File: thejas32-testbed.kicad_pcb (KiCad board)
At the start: 4 copper layers, 81.4 x 89.2 mm, 100 parts, among them J1 Conn_01x04, J10 Conn_02x10_Odd_Even, J11 Conn_01x03, J12 Conn_02x20_Odd_Even, J13 Conn_01x03, J2 USB_B_Micro, J3 Conn_02x03_Odd_Even, J4 Conn_02x05_Odd_Even, J6 Conn_01x10, J7 Conn_01x05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

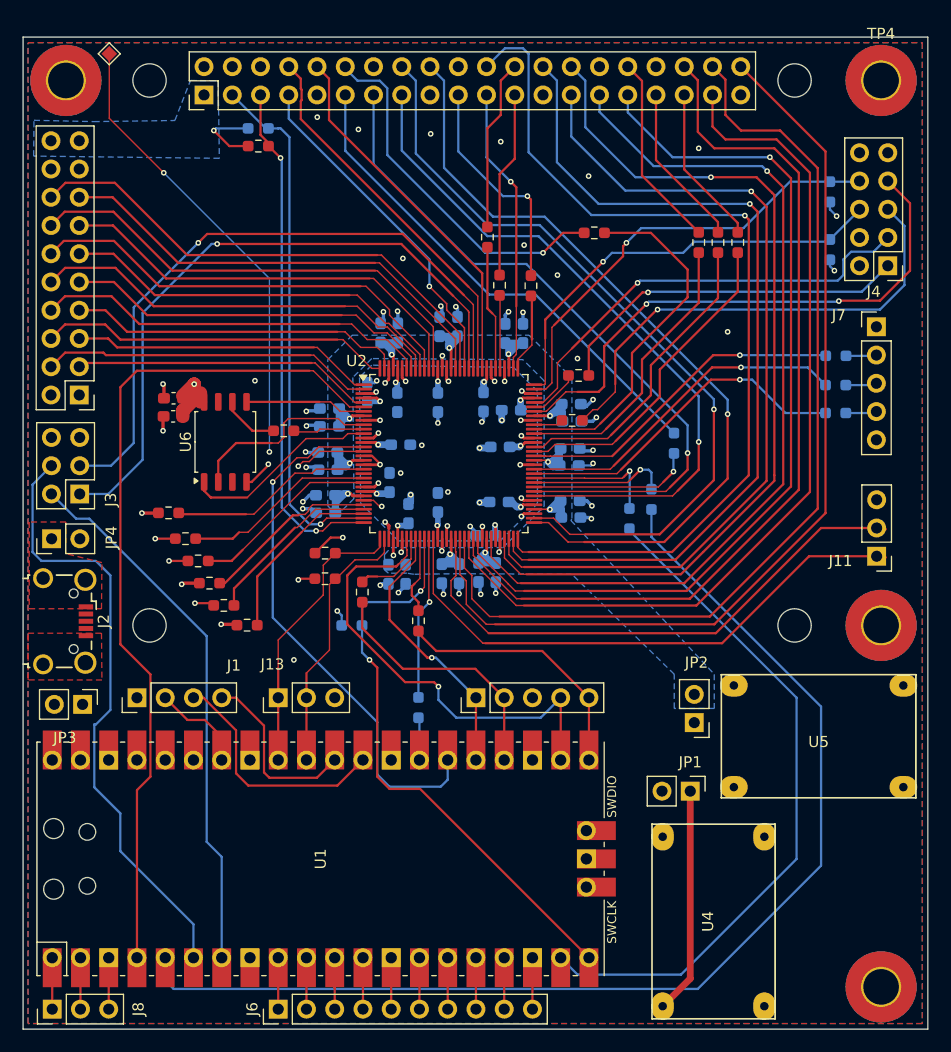
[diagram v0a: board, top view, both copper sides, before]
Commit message: Heartbeat moved near mini360s
Also corrected the file path of the 3D model for the
flash IC
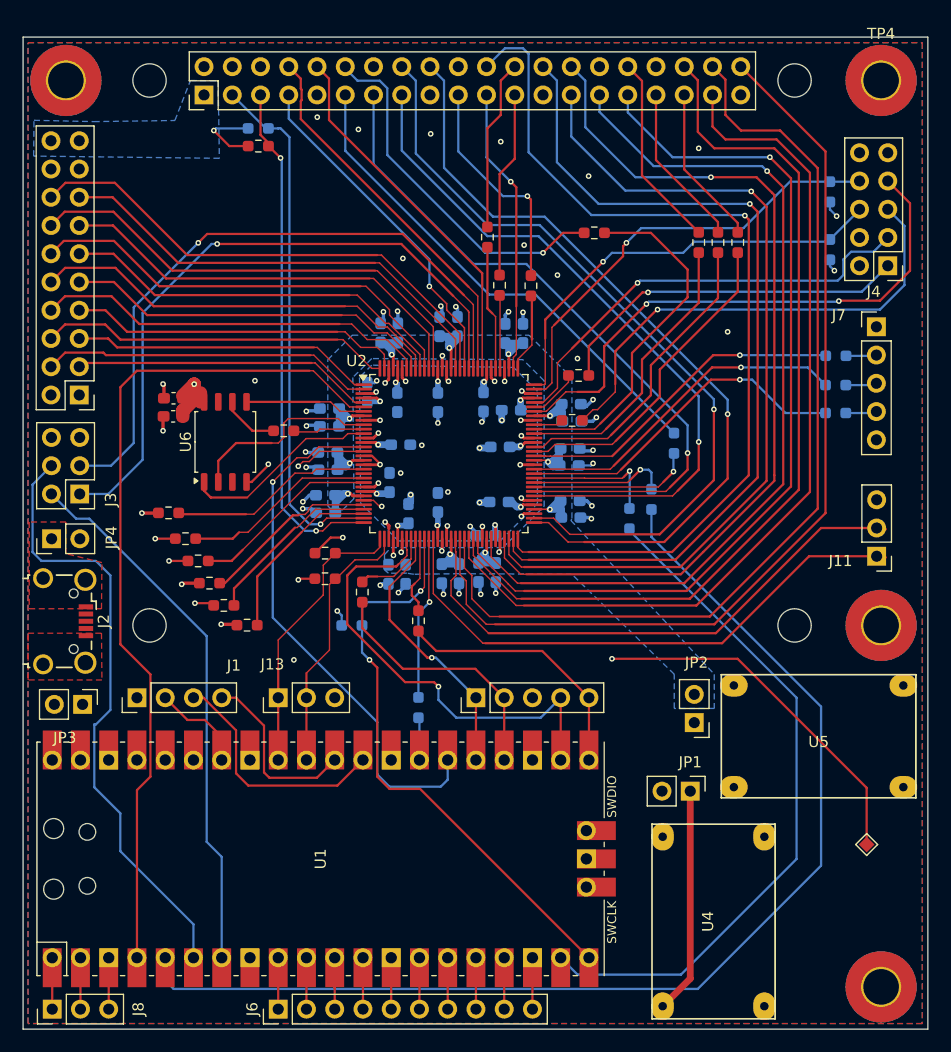
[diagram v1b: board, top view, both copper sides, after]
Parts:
- moved TP7 98.5 mm to (193.1, 139.2)
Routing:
- net Net-(U2-PROC_HEART_BEAT): track 51.3 -> 83.0 mm, vias 3 -> 2
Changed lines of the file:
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@@
 	(footprint "TestPoint:TestPoint_Pad_1.0x1.0mm"
 		(layer "F.Cu")
-		(at 125 68.1 45)
+		(at 193.1 139.2 45)
 		(descr "SMD rectangular pad as test Point, square 1.0mm side length")
 		(tags "test point SMD pad rectangle square")
@@
 		)
 		(property "Footprint" "Package_SO:SOIC-8_5.23x5.23mm_P1.27mm"
-			(at 0 0 90)
+			(at 0.5 -11 90)
 			(unlocked yes)
 			(layer "F.Fab")
@@
 		)
 		(property "Datasheet" "http://www.winbond.com/resource-files/w25q32jv%20revg%2003272018%20plus.pdf"
-			(at 0 0 90)
+			(at 0.5 -6.5 90)
 			(unlocked yes)
 			(layer "F.Fab")
@@
 		)
 		(property "Description" "16Mb Serial Flash Memory, Standard/Dual/Quad SPI, SOIC-8"
-			(at 0 0 90)
+			(at 0.5 -15 90)
 			(unlocked yes)
 			(layer "F.Fab")
@@
 			(pintype "power_in")
 		)
-		(model "${KICAD7_3DMODEL_DIR}/Package_SO.3dshapes/SOIC-8_5.23x5.23mm_P1.27mm.wrl"
+		(model "${KICAD_3DMODEL_DIR}/Package_SO.3dshapes/SOIC-8_5.275x5.275mm_P1.27mm.wrl"
 			(offset
 				(xyz 0 0 0)
@@
 	)
 	(segment
-		(start 125 73.9)
-		(end 125 68.1)
-		(width 0.127)
+		(start 193.1 134.1)
+		(end 193.1 139.2)
+		(width 0.2032)
+		(layer "F.Cu")
+		(net 124)
+	)
+	(segment
+		(start 181.5 122.5)
+		(end 193.1 134.1)
+		(width 0.2032)
 		(layer "F.Cu")
 		(net 124)
@@
 	)
 	(segment
-		(start 142.986756 104.7666)
-		(end 143.900856 103.8525)
-		(width 0.127)
+		(start 170.2 122.5)
+		(end 181.5 122.5)
+		(width 0.2032)
 		(layer "F.Cu")
 		(net 124)
 	)
 	(segment
-		(start 129.9 78.8)
-		(end 125 73.9)
+		(start 142.986756 104.7666)
+		(end 143.900856 103.8525)
 		(width 0.127)
 		(layer "F.Cu")
@@
 	)
 	(via
-		(at 129.9 78.8)
+		(at 141.996208 105.184898)
 		(size 0.508)
 		(drill 0.254)
@@
 	)
 	(via
-		(at 141.996208 105.184898)
+		(at 170.2 122.5)
 		(size 0.508)
 		(drill 0.254)
@@
 		(net 124)
 	)
-	(via
-		(at 139.4 103.9)
-		(size 0.508)
-		(drill 0.254)
-		(layers "F.Cu" "B.Cu")
+	(segment
+		(start 141.8412 117.6412)
+		(end 153.250937 117.6412)
+		(width 0.2032)
+		(layer "In2.Cu")
 		(net 124)
 	)
 	(segment
-		(start 139.4 103.9)
-		(end 140.684898 105.184898)
-		(width 0.127)
+		(start 170.1 122.5)
+		(end 170.2 122.5)
+		(width 0.2032)
 		(layer "In2.Cu")
 		(net 124)
 	)
 	(segment
-		(start 140.684898 105.184898)
-		(end 141.996208 105.184898)
-		(width 0.127)
+		(start 140.9 106.2)
+		(end 140.9 116.7)
+		(width 0.2032)
 		(layer "In2.Cu")
 		(net 124)
 	)
 	(segment
-		(start 139.4 103.9)
-		(end 139.4 88.3)
-		(width 0.127)
-		(layer "B.Cu")
+		(start 165.5588 117.9588)
+		(end 170.1 122.5)
+		(width 0.2032)
+		(layer "In2.Cu")
 		(net 124)
 	)
 	(segment
-		(start 139.4 88.3)
-		(end 129.9 78.8)
-		(width 0.127)
-		(layer "B.Cu")
+		(start 153.568537 117.9588)
+		(end 165.5588 117.9588)
+		(width 0.2032)
+		(layer "In2.Cu")
+		(net 124)
+	)
+	(segment
+		(start 141.996208 105.184898)
+		(end 141.915102 105.184898)
+		(width 0.2032)
+		(layer "In2.Cu")
+		(net 124)
+	)
+	(segment
+		(start 140.9 116.7)
+		(end 141.8412 117.6412)
+		(width 0.2032)
+		(layer "In2.Cu")
+		(net 124)
+	)
+	(segment
+		(start 141.915102 105.184898)
+		(end 140.9 106.2)
+		(width 0.2032)
+		(layer "In2.Cu")
+		(net 124)
+	)
+	(segment
+		(start 153.250937 117.6412)
+		(end 153.568537 117.9588)
+		(width 0.2032)
+		(layer "In2.Cu")
 		(net 124)
 	)
@@
 			(pts
 				(xy 163.3 98.766666) (xy 163.3 108.8) (xy 160.368182 111.8) (xy 150.75 111.8) (xy 145.2 114.8875)
-				(xy 142.6 117.4) (xy 140.4 116.9) (xy 141.5 115) (xy 143.6125 113) (xy 145.7 111.2) (xy 147.45 107.75)
+				(xy 143.5 116.5) (xy 141.4 116.5) (xy 141.4 114.9) (xy 143.6125 113) (xy 145.7 111.2) (xy 147.45 107.75)
 				(xy 147.45 97.924418) (xy 149.3 96.45) (xy 161.295195 96.45)
 			)

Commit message: Cleanup and beautification for review.
Added silkscreen for all components.
Grouped schematic for reading clarity.
No circuit level changes, few nets renamed.
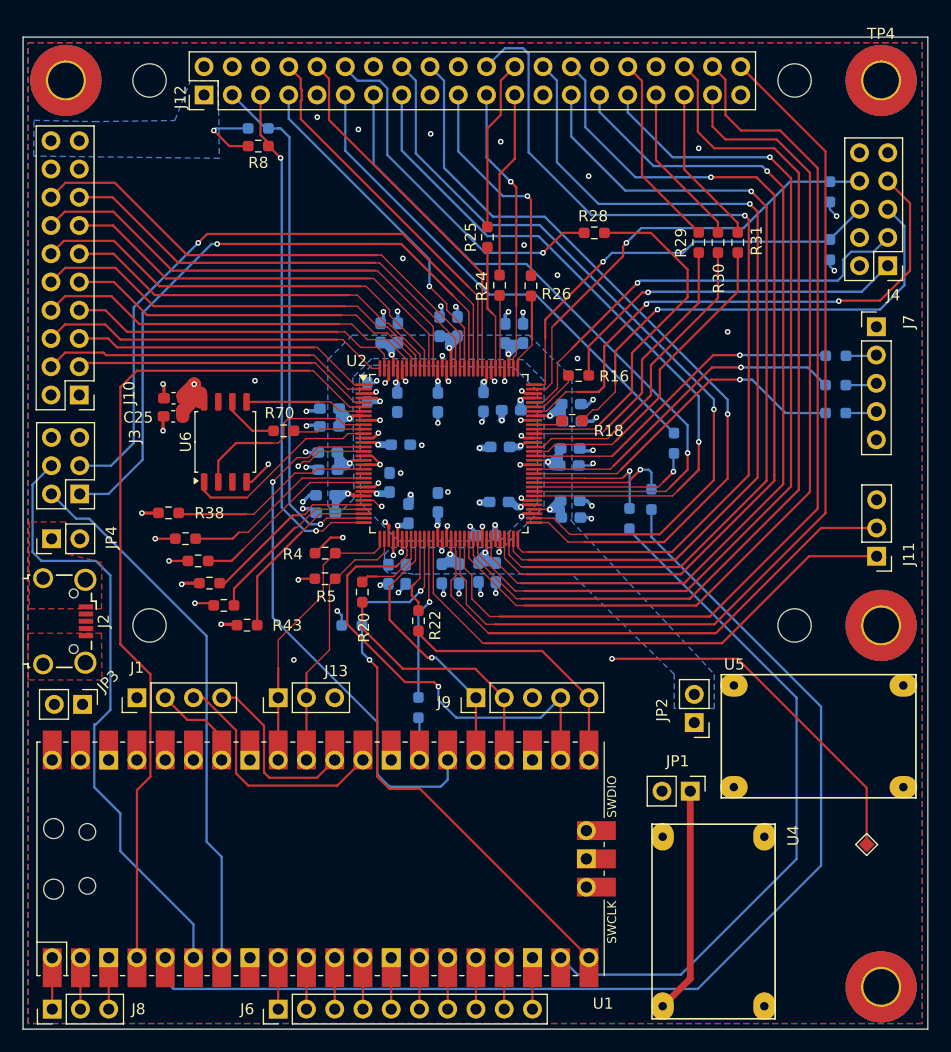
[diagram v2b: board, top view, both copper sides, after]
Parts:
- R1, R70: value 27E -> 10E
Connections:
- net Net-(J11-Pin_1) renamed MCU_UART1_TX
- net Net-(J11-Pin_2) renamed MCU_UART1_RX
- J3 pad 1: Net-(J3-Pin_1) -> MCU_BOOT_UART_TX
- J3 pad 2: MCU_BOOT_UART_TX -> MCU_BOOT_UART_TX_PICO
- J3 pad 3: Net-(J3-Pin_3) -> MCU_BOOT_UART_RX
- J3 pad 4: MCU_BOOT_UART_RX -> MCU_BOOT_UART_RX_PICO
- U1 pad 6: MCU_BOOT_UART_RX -> MCU_BOOT_UART_RX_PICO
- U1 pad 7: MCU_BOOT_UART_TX -> MCU_BOOT_UART_TX_PICO
- U2 pad 107: Net-(J3-Pin_3) -> MCU_BOOT_UART_RX
- U2 pad 108: Net-(J3-Pin_1) -> MCU_BOOT_UART_TX
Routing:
- net Net-(J3-Pin_1): track 59.7 -> 0.00 mm, vias 1 -> 0
- net Net-(J3-Pin_3): track 59.5 -> 0.00 mm, vias 1 -> 0
- net MCU_BOOT_UART_RX_PICO: track 0.00 -> 55.1 mm
- net MCU_BOOT_UART_TX_PICO: track 0.00 -> 48.7 mm
- net MCU_BOOT_UART_TX: track 48.7 -> 59.7 mm, vias 0 -> 1
- net MCU_BOOT_UART_RX: track 55.1 -> 59.5 mm, vias 0 -> 1
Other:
- board text added: "14x GPIOs"
- board text added: "3V3"
- board text added: "4"
- board text added: "5"
- board text added: "6"
- board text added: "ADC2"
- board text added: "BOOT"
- board text added: "BOOT_SEL"
- board text added: "CSN"
- board text added: "GND"
- board text added: "GPIO22"
- board text added: "I2C0"
- board text added: "I2C1"
- board text added: "JTAG"
- board text added: "MCU CLK"
- board text added: "MISO"
- board text added: "MOSI"
- board text added: "NC"
- board text added: "PWM #"
- board text added: "RESET"
- board text added: "RPi HAT Connector"
- board text added: "RUN"
- board text added: "RX"
- board text added: "Raspberry Pi Pico"
- board text added: "SCK"
- board text added: "SCL"
- board text added: "SDA"
- board text added: "SPI"
- board text added: "SPI1"
- board text added: "THEJAS32"
- board text added: "TX"
- board text added: "UART0"
- board text added: "UART1"

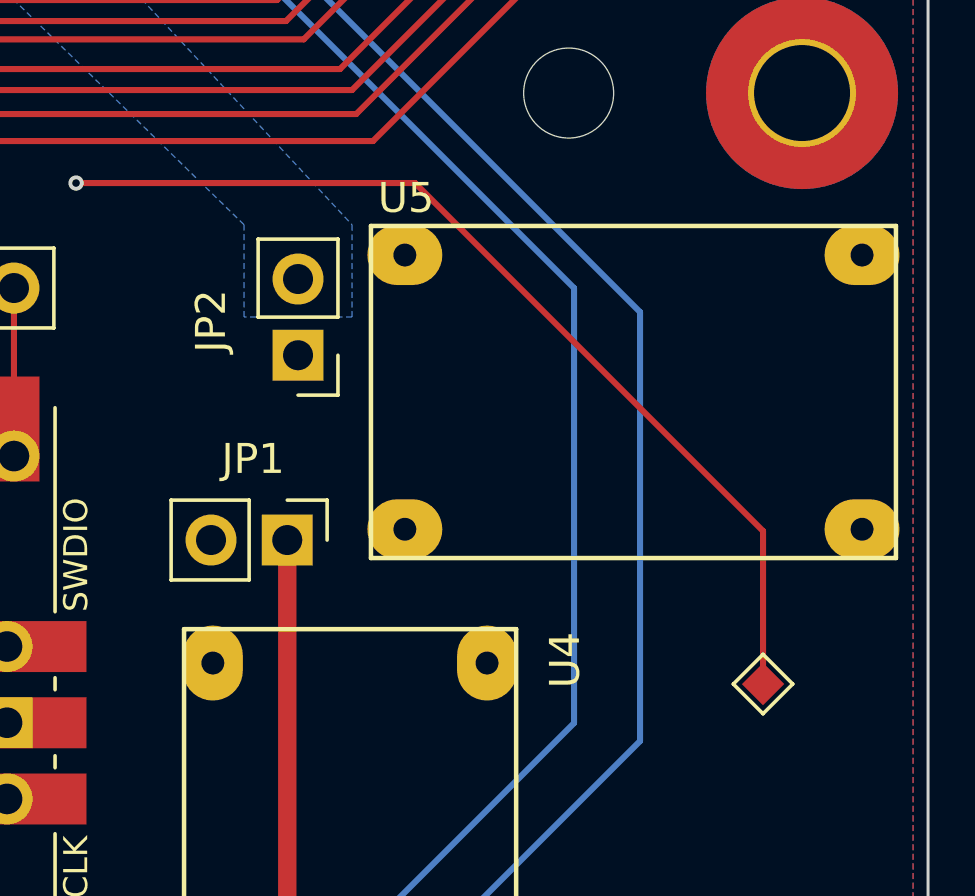
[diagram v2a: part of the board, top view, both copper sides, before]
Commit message: Ready for review, all comments included
All MPNs are provided
Silkscreen updated
BOM generation corrected.
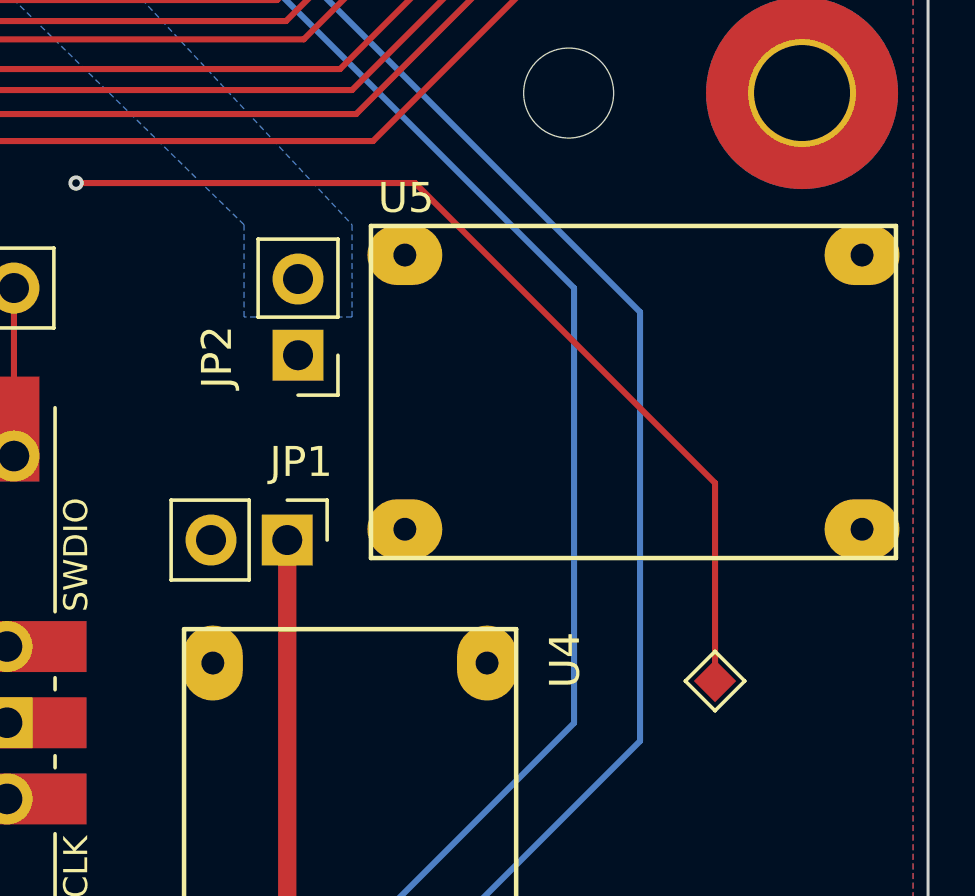
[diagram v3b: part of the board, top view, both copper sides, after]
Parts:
- moved TP7 1.60 mm to (191.5, 139.1)
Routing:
- net Net-(U2-PROC_HEART_BEAT): track 83.0 -> 82.2 mm
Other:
- board text added: "1V2"
- board text added: "Beat"
- board text added: "Heart"
- board text added: "Input 5V"
- board text added: "Mini360"
- board text added: "Output 1V2"
- board text added: "Output 3V3"

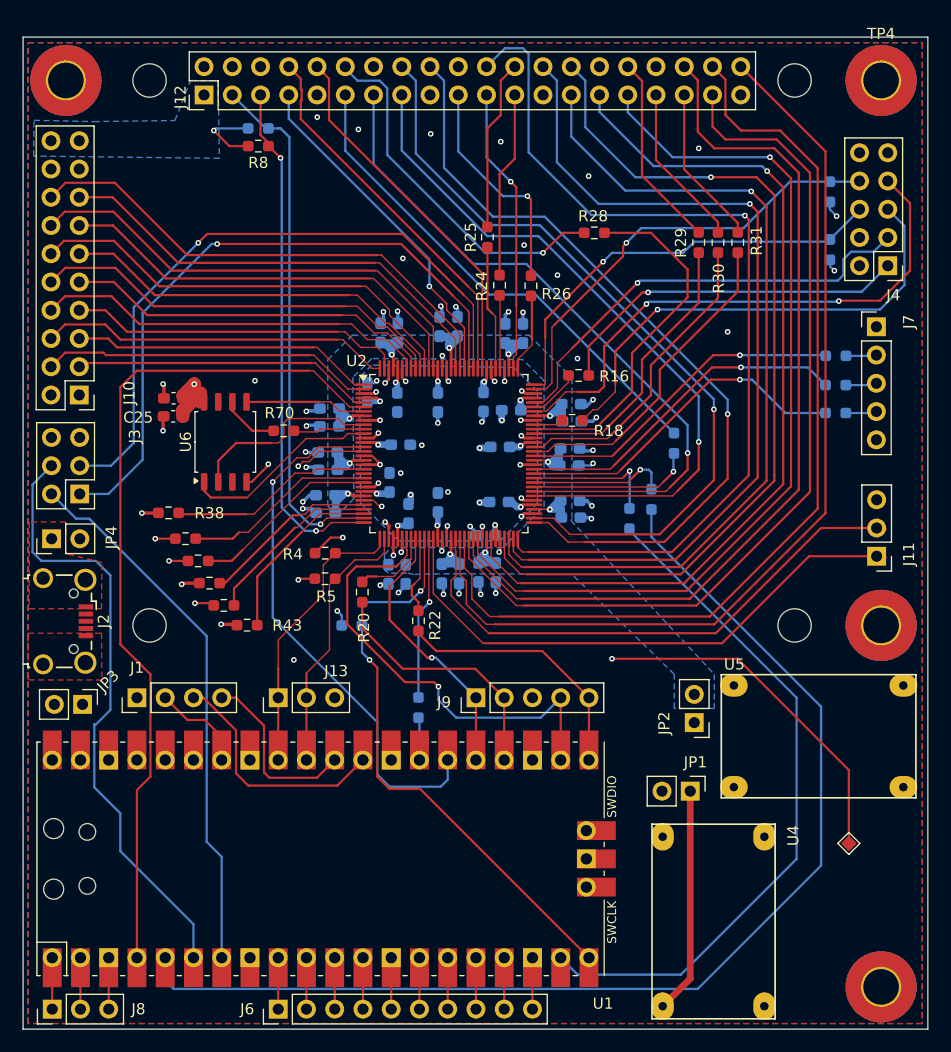
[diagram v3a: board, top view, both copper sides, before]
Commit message: Updates from review
Some major changes:
1. JTAG connector
2. Cleaned up layout in breakout area
3. Improved MCU_CLOCK routing
4. Alignment on right side jumpers
5. 5V included in J10
6. Ground guarding vias around edge

Ref: review of July 20

Updates the silkscreen as well
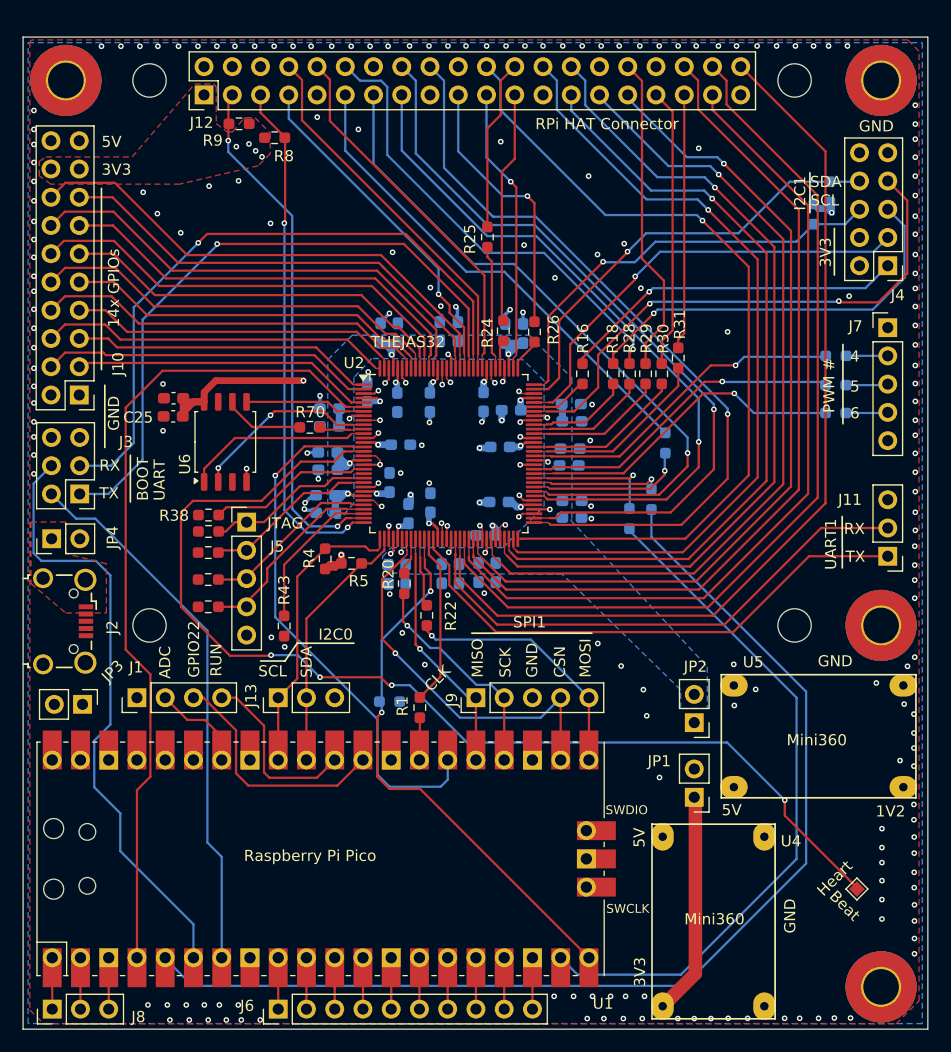
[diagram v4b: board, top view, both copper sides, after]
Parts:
- added J5: Conn_01x05, Connector_PinHeader_2.54mm:PinHeader_1x05_P2.54mm_Vertical, F.Cu at (137.3, 110.2)
- R1, R9: moved to F.Cu
- moved R28 13.1 mm to (171.8, 96.9), turned to 90 degrees
- moved R30 12.8 mm to (174.7, 96.9)
- moved R29 12.7 mm to (173.2, 96.9)
- moved R31 11.7 mm to (176.2, 95.5)
- moved R2 7.64 mm to (150.2, 126.3), turned to 0 degrees
- moved R18 5.58 mm to (170.3, 96.9), turned to 90 degrees
- moved TP7 4.16 mm to (192.2, 143.2)
- moved R26 4.16 mm to (163.2, 93.1)
- moved R24 4.11 mm to (160.4, 93.0)
- moved R20 3.86 mm to (151.5, 115.7)
- moved R38 3.60 mm to (133.9, 109.6)
- moved R6 3.52 mm to (188.3, 82.5), turned to -90 degrees
- moved R43 3.34 mm to (140.7, 119.5), turned to 90 degrees
- moved R5 2.74 mm to (146.8, 113.9)
- moved R70 2.37 mm to (143.0, 101.7)
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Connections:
- J10 pad 17: unconnected-(J10-Pin_17-Pad17) -> PWR_3V3
- J10 pad 18: unconnected-(J10-Pin_18-Pad18) -> PWR_3V3
- J10 pad 19: PWR_3V3 -> PWR_5V
- J10 pad 20: PWR_3V3 -> PWR_5V
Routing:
- net GND: track 98.6 -> 70.8 mm, vias 82 -> 233
- net PWR_1V2: track 64.1 -> 37.8 mm
- net Net-(U2-PWM0): track 31.8 -> 10.7 mm
- net Net-(U2-PROC_HEART_BEAT): track 82.2 -> 99.4 mm, vias 2 -> 4
- net Net-(U2-PWM1): track 25.9 -> 12.4 mm
- net Net-(U2-PWM2): track 27.7 -> 14.2 mm
- net Net-(U2-PWM3): track 29.2 -> 17.0 mm
- net RPi_COMPAT_PWM0_ALT: track 17.5 -> 28.7 mm
- net RPi_COMPAT_PWM1: track 14.7 -> 25.2 mm
- net RPi_COMPAT_PWM0: track 32.6 -> 41.8 mm
- net RPi_COMPAT_GPIO_25: track 83.4 -> 74.5 mm
- net RPi_COMPAT_PWM1_ALT: track 14.3 -> 23.0 mm
- net PWR_3V3: track 185.8 -> 177.9 mm
- net MCU_SPI0_MOSI: track 43.6 -> 36.7 mm
- net Net-(U2-SPI0_MOSI): track 2.67 -> 9.20 mm
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- added copper zone on In1.Cu, net GND
- added copper zone on F.Cu, net PWR_3V3
- removed copper zone on B.Cu, net PWR_3V3
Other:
- board text added: "5V"
- board text added: "ADC"
- board text added: "CLK"
- board text added: "UART"
- board text removed: "ADC2"
- board text removed: "Input 5V"
- board text removed: "MCU CLK"
- board text removed: "NC"
- board text removed: "Output 1V2"
- board text removed: "Output 3V3"
- board text removed: "SPI"
